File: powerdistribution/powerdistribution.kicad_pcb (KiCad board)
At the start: 4 copper layers, 100 x 100 mm, 85 parts, among them IC1 NCP718ASNADJT1G, J1 282837-2, J2 282837-2, J3 M20-6102045, Q1 IRLML0030, Q2 IRLML0030, Q3 IRLML0030, Q5 IRLML0030, U1 BQ7790512PW, U4 AP64501QSP-13, U5 TPS1HC30BQPWPRQ1, U6 TPS1HC30BQPWPRQ1, U7 ESP32-DEVKIT-V1, U9 MIC29302AWD-TR

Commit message: updated pyro
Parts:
- added C11: 10uf, Capacitor_SMD:C_0603_1608Metric_Pad1.08x0.95mm_HandSolder, F.Cu at (181.7, 28.4)
- added C12: 10nf, Capacitor_SMD:C_0603_1608Metric_Pad1.08x0.95mm_HandSolder, F.Cu at (181.7, 31.0)
- added C13: 100nF, Capacitor_SMD:C_0603_1608Metric_Pad1.08x0.95mm_HandSolder, F.Cu at (181.7, 33.5)
- added C14: 33pf, Capacitor_SMD:C_0603_1608Metric_Pad1.08x0.95mm_HandSolder, F.Cu at (181.7, 36.0)
- added C17: 2.7nf, Capacitor_SMD:C_0603_1608Metric_Pad1.08x0.95mm_HandSolder, F.Cu at (181.7, 38.5)
- added C18: 22 uf, Capacitor_SMD:C_0603_1608Metric_Pad1.08x0.95mm_HandSolder, F.Cu at (181.7, 41.0)
- added C19: 22 uf, Capacitor_SMD:C_0603_1608Metric_Pad1.08x0.95mm_HandSolder, F.Cu at (186.1, 25.9)
- added C20: 22uf, Capacitor_SMD:C_0603_1608Metric_Pad1.08x0.95mm_HandSolder, F.Cu at (186.1, 28.4)
- added C25: 33pf, Capacitor_SMD:C_0603_1608Metric_Pad1.08x0.95mm_HandSolder, F.Cu at (186.1, 31.0)
- added C5: 10uf, Capacitor_SMD:C_0603_1608Metric_Pad1.08x0.95mm_HandSolder, F.Cu at (181.7, 25.9)
- added L2: 6.8 uh, Inductor_SMD:L_0603_1608Metric_Pad1.05x0.95mm_HandSolder, F.Cu at (186.1, 33.5)
- added R12: 10.5k, Resistor_SMD:R_0603_1608Metric_Pad0.98x0.95mm_HandSolder, F.Cu at (186.1, 36.0)
- added R13: 31.6k, Resistor_SMD:R_0603_1608Metric_Pad0.98x0.95mm_HandSolder, F.Cu at (186.1, 38.5)
- added R14: 10k, Resistor_SMD:R_0603_1608Metric_Pad0.98x0.95mm_HandSolder, F.Cu at (186.1, 41.0)
- added R30: 5k, Resistor_SMD:R_0603_1608Metric_Pad0.98x0.95mm_HandSolder, F.Cu at (190.4, 25.9)
- added R48: 10k, Resistor_SMD:R_0603_1608Metric_Pad0.98x0.95mm_HandSolder, F.Cu at (190.4, 28.4)
- added R50: 10k, Resistor_SMD:R_0603_1608Metric_Pad0.98x0.95mm_HandSolder, F.Cu at (190.4, 31.0)
- added R52: 0, Resistor_SMD:R_0603_1608Metric_Pad0.98x0.95mm_HandSolder, F.Cu at (190.4, 33.5)
- added R53: 0, Resistor_SMD:R_0603_1608Metric_Pad0.98x0.95mm_HandSolder, F.Cu at (190.4, 36.0)
- added TP6: TestPoint, Connector_PinHeader_2.54mm:PinHeader_1x01_P2.54mm_Vertical, F.Cu at (194.9, 33.3)
- added U3: AP64501QSP-13, HPRfootprints:SO-8EP_DIO-L, F.Cu at (196.5, 27.9)
- R40, R41: value 10k -> 20k
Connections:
- J1 pad 2: Net-(Q5-S) -> Net-(Q5-D)
- J2 pad 2: Net-(Q3-S) -> Net-(Q3-D)
- Q3 pad 2: Net-(Q3-S) -> GND
- Q3 pad 3: GND -> Net-(Q3-D)
- Q5 pad 2: Net-(Q5-S) -> GND
- Q5 pad 3: GND -> Net-(Q5-D)
- R40 pad 1: unconnected-(R40-Pad1) -> /PYRO1CONN
- R40 pad 2: Net-(Q5-S) -> Net-(Q5-D)
- R41 pad 1: unconnected-(R41-Pad1) -> /PYRO2CONN
- R41 pad 2: Net-(Q3-S) -> Net-(Q3-D)
- R42 pad 1: Net-(Q5-S) -> /PYRO1CONN
- R43 pad 1: Net-(Q3-S) -> /PYRO2CONN

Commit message: update bms parts + board size
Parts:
- removed R44: CSNL2512FT1L00, HPRfootprints:STA_CSNL25121_STP
- added C44: 220nf, Capacitor_SMD:C_0603_1608Metric_Pad1.08x0.95mm_HandSolder, F.Cu at (119.9, 151.3)
- added C45: 220nf, Capacitor_SMD:C_0603_1608Metric_Pad1.08x0.95mm_HandSolder, F.Cu at (124.3, 136.2)
- added J6: Conn_01x02, Connector_PinHeader_2.54mm:PinHeader_1x02_P2.54mm_Vertical, F.Cu at (141.5, 147.0)
- added M1: Motor_Servo, Connector_PinHeader_2.54mm:PinHeader_1x03_P2.54mm_Vertical, F.Cu at (137.4, 137.3)
- added M2: Motor_Servo, Connector_PinHeader_2.54mm:PinHeader_1x03_P2.54mm_Vertical, F.Cu at (142.0, 137.3)
- added R16: R_Small, Resistor_SMD:R_0603_1608Metric_Pad0.98x0.95mm_HandSolder, F.Cu at (124.3, 148.8)
- added R56: 10k, Resistor_SMD:R_0603_1608Metric_Pad0.98x0.95mm_HandSolder, F.Cu at (128.6, 136.2)
- added R57: 10k, Resistor_SMD:R_0603_1608Metric_Pad0.98x0.95mm_HandSolder, F.Cu at (128.6, 138.8)
- added R58: 10k, Resistor_SMD:R_0603_1608Metric_Pad0.98x0.95mm_HandSolder, F.Cu at (128.6, 141.3)
- added R59: 10k, Resistor_SMD:R_0603_1608Metric_Pad0.98x0.95mm_HandSolder, F.Cu at (128.6, 143.8)
- added R6: R_Small, Resistor_SMD:R_0603_1608Metric_Pad0.98x0.95mm_HandSolder, F.Cu at (124.3, 138.8)
- added R60: 5k, Resistor_SMD:R_0603_1608Metric_Pad0.98x0.95mm_HandSolder, F.Cu at (128.6, 146.3)
- added R61: 5k, Resistor_SMD:R_0603_1608Metric_Pad0.98x0.95mm_HandSolder, F.Cu at (128.6, 148.8)
- added R62: 5k, Resistor_SMD:R_0603_1608Metric_Pad0.98x0.95mm_HandSolder, F.Cu at (128.6, 151.3)
- added R63: 5k, Resistor_SMD:R_0603_1608Metric_Pad0.98x0.95mm_HandSolder, F.Cu at (133.0, 136.2)
- added R64: ~, Resistor_SMD:R_0603_1608Metric_Pad0.98x0.95mm_HandSolder, F.Cu at (133.0, 138.8)
- added R65: 1k, Resistor_SMD:R_0603_1608Metric_Pad0.98x0.95mm_HandSolder, F.Cu at (133.0, 141.3)
- added R66: 5k, Resistor_SMD:R_0603_1608Metric_Pad0.98x0.95mm_HandSolder, F.Cu at (133.0, 143.8)
- added R67: R_Small, Resistor_SMD:R_0603_1608Metric_Pad0.98x0.95mm_HandSolder, F.Cu at (133.0, 146.3)
- added TP7: TestPoint, Connector_PinHeader_2.00mm:PinHeader_1x01_P2.00mm_Vertical, F.Cu at (137.2, 146.7)
- added TP8: TestPoint, Connector_PinHeader_2.00mm:PinHeader_1x01_P2.00mm_Vertical, F.Cu at (137.2, 150.7)
- added U10: TPS1HC30BQPWPRQ1, HPRfootprints:IC_TPS1HC30BQPWPRQ1, F.Cu at (123.1, 155.8)
- C1, C2, C3, C4: value C0603C104K5RACTU -> 0.1μF; footprint HPRfootprints:CAPC1608X90 -> Capacitor_SMD:C_0603_1608Metric_Pad1.08x0.95mm_HandSolder
- C37, C38: value UMK107AB7105KA-T -> C_Small; footprint HPRfootprints:CAPC1608X95N -> Capacitor_SMD:C_0603_1608Metric_Pad1.08x0.95mm_HandSolder
- J3: value M20-6102045 -> ESQ-113-12-G-D; footprint HPRfootprints:RHDR40W66P254_2X20_5146X500X1105P -> HPRfootprints:SAMTEC_ESQ-113-12-G-D
- R1, R2, R3, R4, R5: footprint HPRfootprints:R0402 -> Resistor_SMD:R_0603_1608Metric_Pad0.98x0.95mm_HandSolder
- R15, R17: value ERJ2RKF1004X -> R_Small; footprint HPRfootprints:RES_ERJ2RKF1004X -> Resistor_SMD:R_0603_1608Metric_Pad0.98x0.95mm_HandSolder
- R7: value RC1206FR-074K53L -> R_Small; footprint HPRfootprints:RC1206N_YAG -> Resistor_SMD:R_0603_1608Metric_Pad0.98x0.95mm_HandSolder
- R8: value RC0603FR-0710KL -> R_Small; footprint HPRfootprints:RESC1607X60N -> Resistor_SMD:R_0603_1608Metric_Pad0.98x0.95mm_HandSolder
- moved J3 213.3 mm to (218.2, 146.2), turned to 0 degrees
- moved BT1 204.9 mm to (261.1, 88.3), turned to 0 degrees
- moved R5 132.9 mm to (155.4, 147.1), turned to 0 degrees
- moved R4 130.5 mm to (155.4, 144.6), turned to 0 degrees
- moved RT1 129.0 mm to (165.2, 148.8)
- moved R3 125.6 mm to (155.4, 142.1), turned to 0 degrees
- moved C38 124.7 mm to (119.9, 148.8)
- moved U1 123.3 mm to (162.5, 139.9)
- moved C37 121.8 mm to (119.9, 146.3)
- moved Q2 121.0 mm to (160.0, 151.0), turned to 0 degrees
- moved R2 120.6 mm to (155.4, 139.6), turned to 0 degrees
- moved R17 119.2 mm to (124.3, 151.3), turned to 0 degrees
- moved Q1 118.4 mm to (160.0, 146.4), turned to 0 degrees
- moved C4 118.0 mm to (119.9, 143.8)
- moved R1 115.7 mm to (155.4, 137.1), turned to 0 degrees
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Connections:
- C18 pad 1: /6V -> /12V
- C19 pad 1: /6V -> /12V
- C20 pad 1: /6V -> /12V
- C37 pad 1: /AVdd -> Net-(U1-AVDD)
- C38 pad 1: GND -> Net-(U1-VDD)
- C38 pad 2: /Vdd -> GND
- L2 pad 1: /6V -> /12V
- R13 pad 1: /6V -> /12V
- R15 pad 1: /sns- -> Net-(U1-CHG)
- R15 pad 2: Net-(Q1-G) -> Net-(Q2-G)
- R17 pad 1: Net-(Q2-G) -> GND
- R17 pad 2: Net-(U1-CHG) -> /sns-
- R7 pad 1: Net-(Q1-G) -> Net-(U1-DSG)
- R7 pad 2: Net-(U1-DSG) -> Net-(Q1-G)
- R8 pad 1: Net-(U1-TS) -> Net-(U1-VTB)
- R8 pad 2: Net-(U1-VTB) -> Net-(U1-TS)
- U1 pad 1: /Vdd -> Net-(U1-VDD)
- U1 pad 2: /AVdd -> Net-(U1-AVDD)
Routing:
- net /AVdd: track 12.0 -> 0.00 mm
- net /sns-: track 9.74 -> 0.00 mm
- net Net-(U1-VC1): track 6.80 -> 0.00 mm
- net Net-(U1-TS): track 6.49 -> 0.00 mm
- net Net-(U1-DSG): track 6.12 -> 0.00 mm
- net Net-(Q2-G): track 6.12 -> 0.00 mm
- net Net-(U1-VC4): track 5.58 -> 0.00 mm
- net /Vdd: track 5.49 -> 0.00 mm
- net Net-(U1-VC3): track 4.46 -> 0.00 mm
- net Net-(U1-VC2): track 4.45 -> 0.00 mm
- net Net-(Q1-G): track 4.19 -> 0.00 mm
- net Net-(Q1-D): track 3.90 -> 0.00 mm
- net Net-(U1-CHG): track 3.48 -> 0.00 mm
- net /Pack+: track 7.15 -> 4.00 mm
- net Net-(U1-VTB): track 2.60 -> 0.00 mm
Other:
- board size 100 x 100 mm -> 130 x 70 mm

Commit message: update bms to 3 battery
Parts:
- removed C4: 0.1μF, Capacitor_SMD:C_0603_1608Metric_Pad1.08x0.95mm_HandSolder
- removed R4: 1K, Resistor_SMD:R_0603_1608Metric_Pad0.98x0.95mm_HandSolder
- BT1: value BK-18650-PC8 -> BK-18650-PC6; footprint HPRfootprints:BAT_BK-18650-PC8 -> HPRfootprints:BAT_BK-18650-PC6
- moved BT1 183.4 mm to (78.2, 102.0), turned to 180 degrees
- moved C25 154.5 mm to (58.0, 117.3), turned to 180 degrees
- moved R5 124.7 mm to (59.3, 67.7), turned to 180 degrees
- moved RT1 121.5 mm to (73.8, 68.8), turned to 90 degrees
- moved R3 119.7 mm to (59.3, 70.7)
- moved R18 117.6 mm to (63.2, 117.3)
- moved L3 115.5 mm to (66.0, 104.1)
- moved R2 114.4 mm to (59.5, 77.2)
- moved C28 114.4 mm to (68.2, 117.3), turned to 0 degrees
- moved U1 114.0 mm to (67.0, 77.5)
- moved R20 111.2 mm to (73.2, 117.3)
- moved C24 111.0 mm to (60.2, 104.1)
- moved C31 110.1 mm to (71.2, 104.1)
- moved R1 110.0 mm to (59.5, 83.2)
- moved R19 109.9 mm to (73.2, 113.1)
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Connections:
- net /sns- renamed Net-(Q1-S)
- BT1 pad 3+: Net-(BT1-Pad3+) -> /Pack+
- Q2 pad 2: GND -> /Pack-
- R16 pad 2: GND -> /Pack-
- R3 pad 1: Net-(BT1-Pad3+) -> /Pack+
- R5 pad 1: /Vdd -> Net-(U1-VDD)
- R6 pad 1: GND -> /Pack-
- U1 pad 17: /AVdd -> Net-(U1-AVDD)
- U1 pad 3: Net-(U1-VC4) -> Net-(U1-VC3)
- U1 pad 4: Net-(U1-VC4) -> Net-(U1-VC3)
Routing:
- net Net-(U5-ILIM): track 5.74 -> 0.00 mm
- net /6V_EN: track 5.27 -> 0.00 mm
- net /6V_DIAGEN: track 5.18 -> 0.00 mm
- net Net-(U5-EN): track 5.02 -> 0.00 mm
- net Net-(U5-SNS): track 4.83 -> 0.00 mm
- net /Pack+: track 4.00 -> 0.00 mm
- net Net-(U5-LATCH): track 3.54 -> 0.00 mm
- net Net-(U5-DIAG_EN): track 2.88 -> 0.00 mm
- net Net-(U5-~{FAULT}): track 2.48 -> 0.00 mm
- net /6v_cursns: track 2.17 -> 0.00 mm

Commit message: pwr board general placement
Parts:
- moved U3 222.4 mm to (23.1, 167.1)
- moved C12 217.7 mm to (14.9, 170.8)
- moved C11 217.1 mm to (14.9, 167.3)
- moved C14 216.6 mm to (14.9, 174.1)
- moved C5 216.4 mm to (14.9, 163.8)
- moved R12 215.9 mm to (20.1, 174.1)
- moved C13 208.3 mm to (16.7, 160.6)
- moved C19 207.3 mm to (30.7, 163.1), turned to 180 degrees
- moved C17 207.1 mm to (25.2, 174.1)
- moved L2 207.0 mm to (22.7, 160.6)
- moved C20 205.3 mm to (28.8, 160.3), turned to 180 degrees
- moved R14 204.8 mm to (30.4, 174.1)
- moved R13 203.3 mm to (30.6, 169.6), turned to 180 degrees
- moved C18 196.3 mm to (30.7, 166.3), turned to 180 degrees
- moved TP6 152.2 mm to (121.8, 166.8), turned to 90 degrees
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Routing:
- net Net-(BT1-Pad2+): track 0.00 -> 80.9 mm
- net Net-(BT1-Pad1+): track 0.00 -> 80.9 mm
- net Net-(U7-EN): track 0.00 -> 34.3 mm
- net Net-(Q3-D): track 0.00 -> 12.5 mm
- net Net-(Q5-D): track 0.00 -> 11.7 mm
- net /6V: track 6.35 -> 0.00 mm
- net Net-(U9-ADJ): track 5.24 -> 0.00 mm
- net Net-(U5-VOUT): track 4.19 -> 0.00 mm
- net /PYRO2CONN: track 0.00 -> 3.90 mm
- net /PYRO1CONN: track 0.00 -> 3.90 mm
- net /PYRO2: track 0.00 -> 3.33 mm
- net /PYRO1: track 0.00 -> 2.92 mm

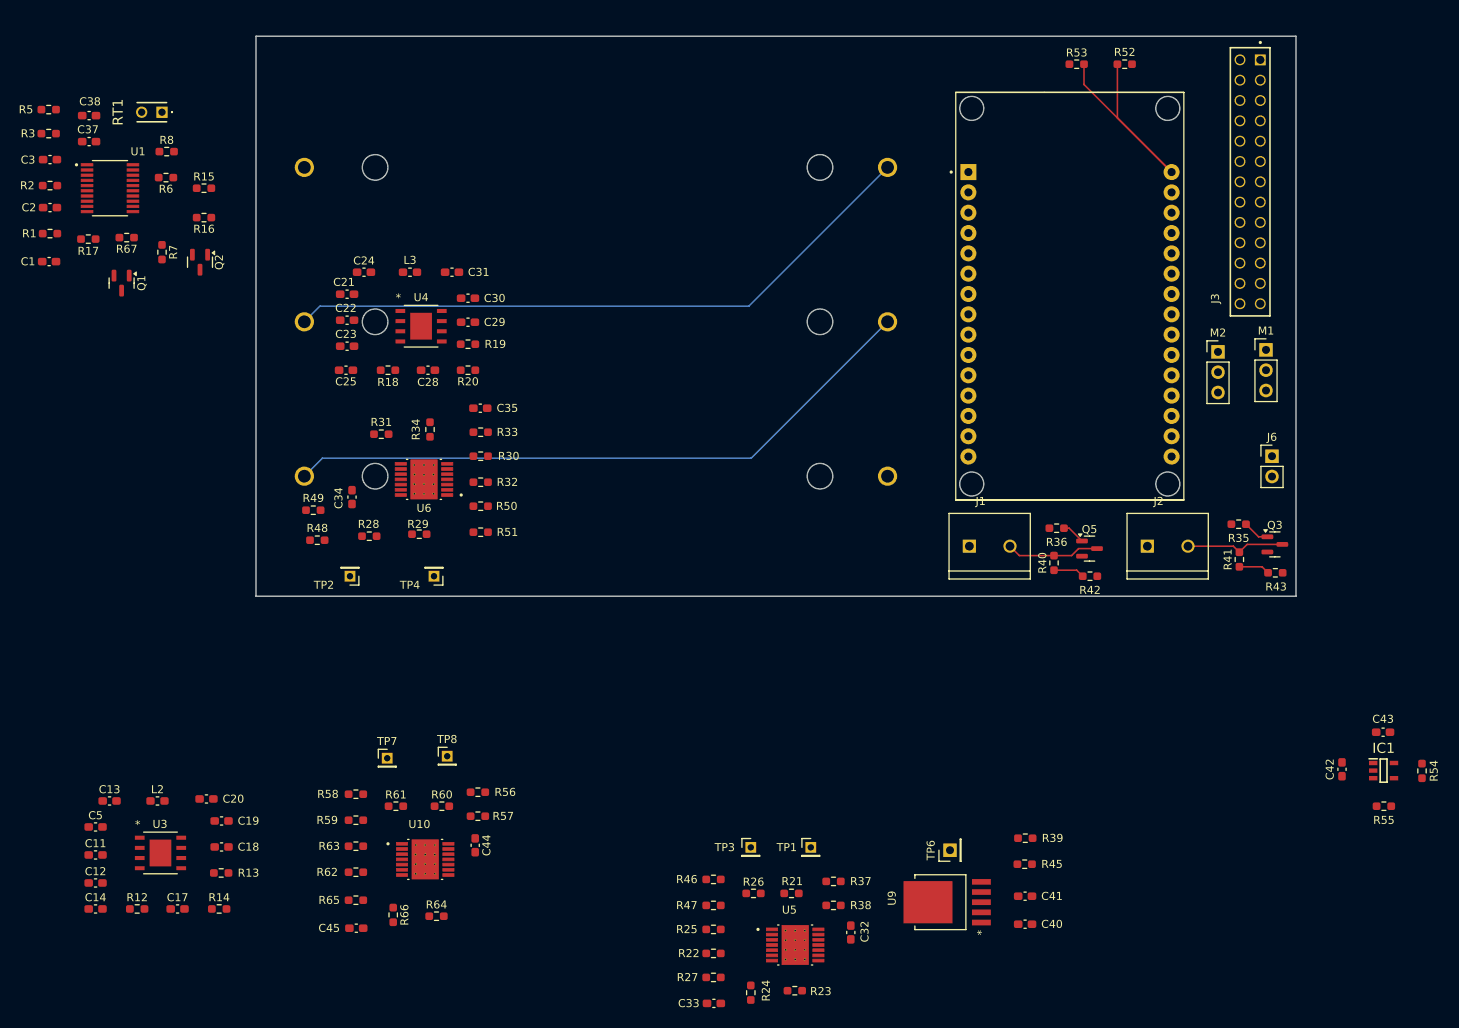
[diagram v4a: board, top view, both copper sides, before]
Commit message: new board size+routing
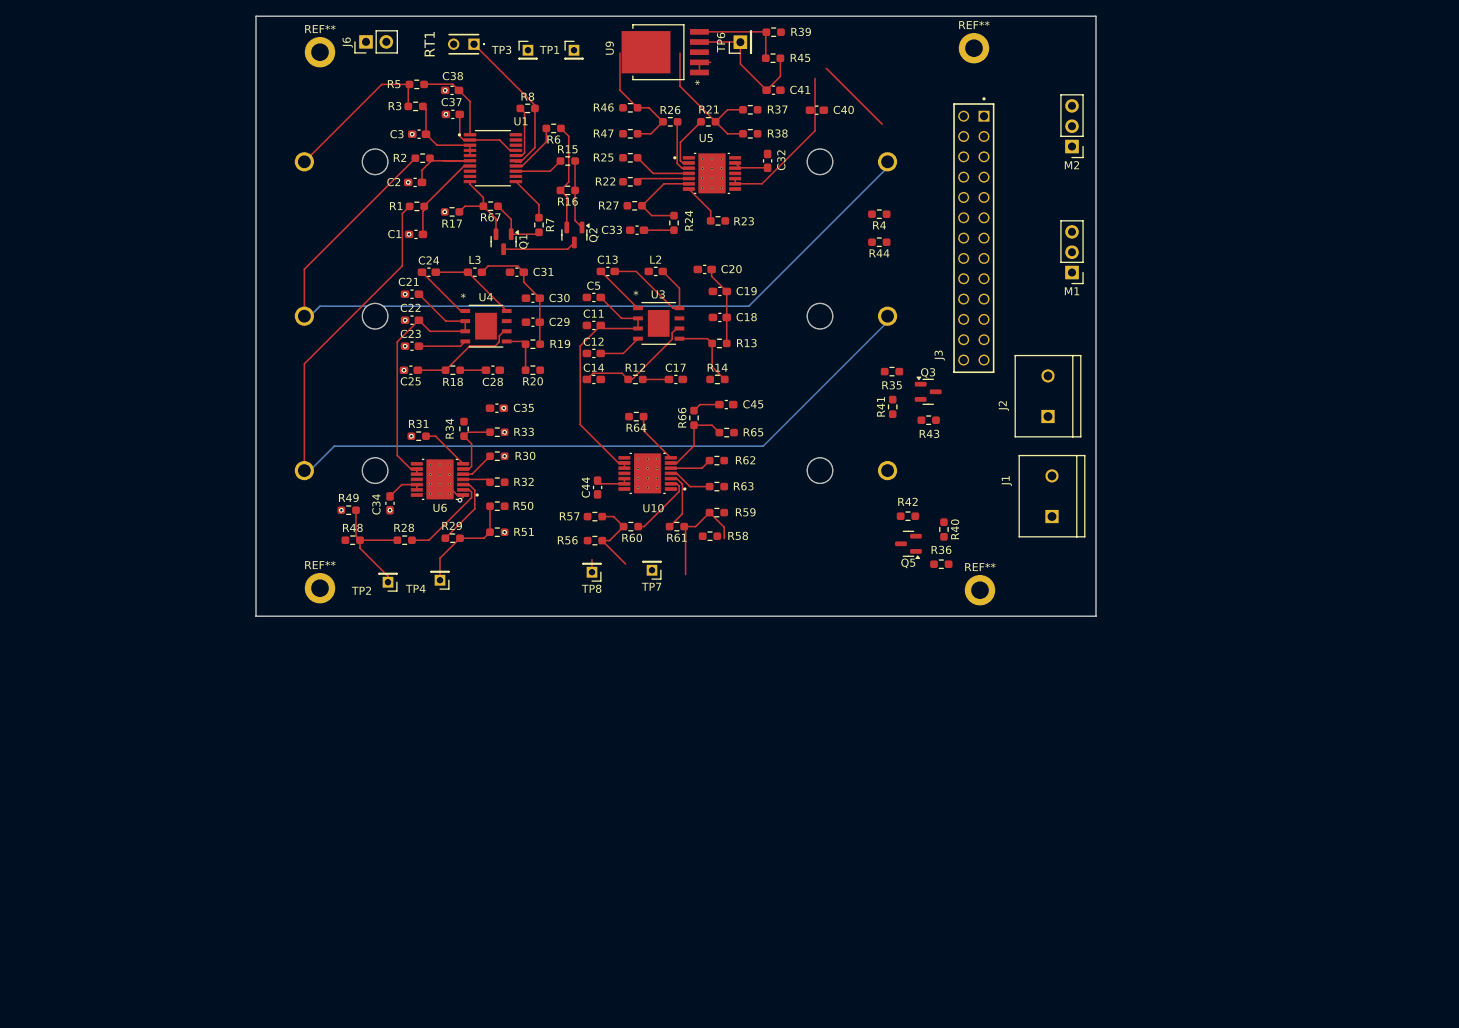
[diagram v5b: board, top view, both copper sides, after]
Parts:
- removed C42, C43: 1uF, Capacitor_SMD:C_0603_1608Metric_Pad1.08x0.95mm_HandSolder
- removed IC1: NCP718ASNADJT1G, HPRfootprints:NCP718_SOT95P280X100-5N
- removed R52, R53: 0, Resistor_SMD:R_0603_1608Metric_Pad0.98x0.95mm_HandSolder
- removed R54: 19k, Resistor_SMD:R_0603_1608Metric_Pad0.98x0.95mm_HandSolder
- removed R55: 6k, Resistor_SMD:R_0603_1608Metric_Pad0.98x0.95mm_HandSolder
- removed U7: ESP32-DEVKIT-V1, HPRfootprints:MODULE_ESP32_DEVKIT_V1
- added R4: 0, Resistor_SMD:R_0603_1608Metric_Pad0.98x0.95mm_HandSolder, F.Cu at (112.9, 87.2)
- added R44: 0, Resistor_SMD:R_0603_1608Metric_Pad0.98x0.95mm_HandSolder, F.Cu at (112.9, 90.8)
- added REF**: MountingHole_2.2mm_M2_DIN965_Pad, MountingHole:MountingHole_2.2mm_M2_DIN965_Pad, F.Cu at (125.5, 134.2)
- added REF**: MountingHole_2.2mm_M2_DIN965_Pad, MountingHole:MountingHole_2.2mm_M2_DIN965_Pad, F.Cu at (124.8, 66.5)
- added REF**: MountingHole_2.2mm_M2_DIN965_Pad, MountingHole:MountingHole_2.2mm_M2_DIN965_Pad, F.Cu at (43.0, 134.0)
- added REF**: MountingHole_2.2mm_M2_DIN965_Pad, MountingHole:MountingHole_2.2mm_M2_DIN965_Pad, F.Cu at (43.0, 67.0)
- moved J6 124.5 mm to (48.8, 65.7), turned to 90 degrees
- moved U9 111.9 mm to (85.3, 67.0)
- moved C41 105.5 mm to (99.7, 71.8)
- moved R39 105.5 mm to (99.7, 64.5)
- moved R45 105.5 mm to (99.6, 67.8)
- moved C40 105.0 mm to (105.1, 74.2)
- moved TP6 104.3 mm to (95.5, 65.8)
- moved TP1 104.0 mm to (74.8, 66.8)
- moved TP3 103.5 mm to (69.0, 66.8)
- moved C33 97.1 mm to (82.6, 89.2)
- moved R21 97.0 mm to (91.5, 75.7)
- moved R22 97.0 mm to (81.8, 83.2)
- moved R25 97.0 mm to (81.8, 80.2)
- moved R26 97.0 mm to (86.8, 75.7)
- moved R37 97.0 mm to (96.8, 74.2)
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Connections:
- J1 pad 1: /VBATT -> /Pack+
- J2 pad 1: /VBATT -> /Pack+
- J3 pad 01: unconnected-(J3-Pad01) -> GND
- J3 pad 02: unconnected-(J3-Pad02) -> Net-(J3-Pad02)
- J3 pad 03: unconnected-(J3-Pad03) -> GND
- J3 pad 04: unconnected-(J3-Pad04) -> Net-(J3-Pad04)
- J3 pad 05: unconnected-(J3-Pad05) -> GND
- J3 pad 06: unconnected-(J3-Pad06) -> /aux7_rx
- J3 pad 07: unconnected-(J3-Pad07) -> GND
- J3 pad 08: unconnected-(J3-Pad08) -> /aux7_tx
- J3 pad 09: unconnected-(J3-Pad09) -> GND
- J3 pad 10: unconnected-(J3-Pad10) -> /can_rx
- J3 pad 11: unconnected-(J3-Pad11) -> GND
- J3 pad 12: unconnected-(J3-Pad12) -> /can_tx
- J3 pad 13: unconnected-(J3-Pad13) -> /5V
- J3 pad 14: unconnected-(J3-Pad14) -> /SENSE_mosi
- J3 pad 15: unconnected-(J3-Pad15) -> /5V
- J3 pad 16: unconnected-(J3-Pad16) -> /SENSE_miso
- J3 pad 17: unconnected-(J3-Pad17) -> /5V
- J3 pad 18: unconnected-(J3-Pad18) -> /SENSE_sck
- J3 pad 19: unconnected-(J3-Pad19) -> /5V
- J3 pad 20: unconnected-(J3-Pad20) -> /servo2_pwm
- J3 pad 21: unconnected-(J3-Pad21) -> /5V
- J3 pad 22: unconnected-(J3-Pad22) -> /servo1_pwm
- J3 pad 23: unconnected-(J3-Pad23) -> /5V
- J3 pad 24: unconnected-(J3-Pad24) -> /PYRO1
- J3 pad 25: unconnected-(J3-Pad25) -> /5V
- J3 pad 26: unconnected-(J3-Pad26) -> /PYRO2
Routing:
- net Net-(BT1-Pad1+): track 80.9 -> 119.4 mm
- net Net-(U4-EN): track 0.00 -> 36.6 mm
- net Net-(U7-EN): track 34.3 -> 0.00 mm
- net Net-(U10-VOUT): track 0.00 -> 33.4 mm
- net /Pack+: track 0.00 -> 33.0 mm
- net Net-(U5-VOUT): track 0.00 -> 32.5 mm
- net /6V_EN: track 0.00 -> 30.8 mm
- net /6V_DIAGEN: track 0.00 -> 29.4 mm
- net Net-(BT1-Pad2+): track 80.9 -> 106.4 mm
- net Net-(U1-TS): track 0.00 -> 19.4 mm
- net /6V: track 0.00 -> 17.2 mm
- net /5V: track 0.00 -> 15.7 mm
- net Net-(U3-SW): track 0.00 -> 15.5 mm
- net /5V_EN: track 0.00 -> 15.3 mm
- net Net-(U3-COMP): track 0.00 -> 15.3 mm
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- added copper zone on In1.Cu, net GND
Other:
- board size 130 x 70 mm -> 105 x 75 mm

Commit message: pd placement
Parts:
- moved R30 32.3 mm to (97.4, 118.0)
- moved R28 32.3 mm to (85.8, 127.6)
- moved R29 32.3 mm to (91.8, 127.3)
- moved R31 32.3 mm to (87.6, 114.6)
- moved R48 32.3 mm to (79.3, 127.6)
- moved R49 32.3 mm to (78.8, 123.8)
- moved C34 32.3 mm to (84.0, 123.0)
- moved C35 32.3 mm to (97.4, 111.1)
- moved R32 32.3 mm to (97.4, 120.3)
- moved R33 32.3 mm to (97.4, 114.1)
- moved R34 32.3 mm to (93.2, 113.7)
- moved R50 32.3 mm to (97.4, 123.3)
- moved R51 32.3 mm to (97.4, 126.6)
- moved TP2 32.3 mm to (83.8, 132.8)
- moved TP4 32.3 mm to (90.2, 132.6)
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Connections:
- R56 pad 1: /6V_EN -> /12V_EN
- R57 pad 2: /6V_EN -> /12V_EN
- R58 pad 1: /6V_DIAGEN -> /12V_DIAGEN
- R59 pad 2: /6V_DIAGEN -> /12V_DIAGEN
- R60 pad 1: /6V_EN -> /12V_EN
- R61 pad 1: /6V_DIAGEN -> /12V_DIAGEN
- TP7 pad 1: /6V_DIAGEN -> /12V_DIAGEN
- TP8 pad 1: /6V_EN -> /12V_EN
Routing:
- net /LDO_5V: track 0.00 -> 64.9 mm, vias 0 -> 6
- net /6V: track 17.2 -> 70.2 mm
- net /5V: track 15.7 -> 62.5 mm
- net /PYRO1: track 0.00 -> 28.8 mm, vias 0 -> 1
- net Net-(Q5-D): track 0.00 -> 28.2 mm
- net GND: track 4.87 -> 30.8 mm, vias 18 -> 62
- net /servo2_pwm: track 0.00 -> 24.1 mm
- net /Pack+: track 33.0 -> 13.8 mm, vias 0 -> 5
- net Net-(Q3-D): track 0.00 -> 17.5 mm
- net /12V_DIAGEN: track 0.00 -> 14.4 mm
- net /servo1_pwm: track 0.00 -> 14.1 mm
- net /PYRO2: track 0.00 -> 12.0 mm, vias 0 -> 1
- net /12V_EN: track 0.00 -> 11.1 mm
- net /12V: track 10.0 -> 18.6 mm
- net /6V_DIAGEN: track 29.4 -> 23.7 mm
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- added copper zone on In2.Cu, net /Pack+
